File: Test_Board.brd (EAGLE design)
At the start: 63.5 x 57.1 mm, 33 parts, among them U1 Value, U2 Value

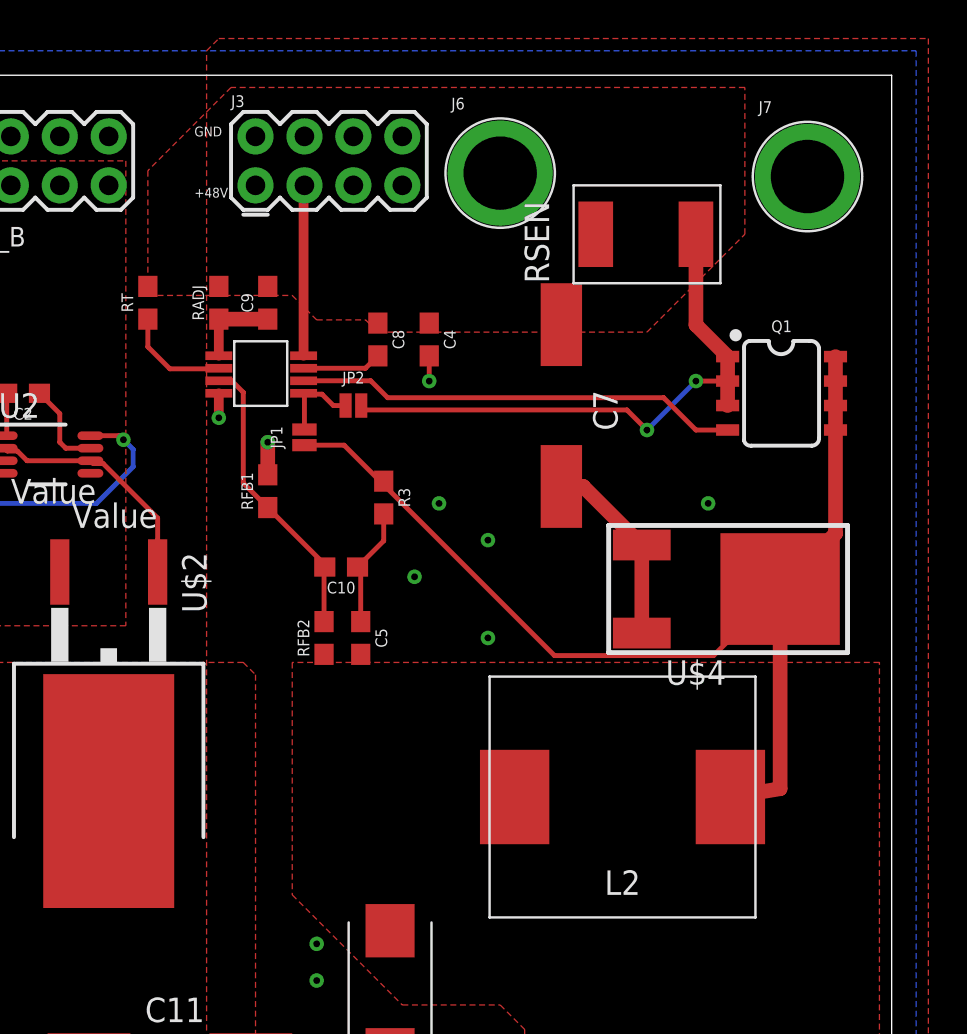
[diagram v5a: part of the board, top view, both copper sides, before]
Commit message: adjusted buck controller
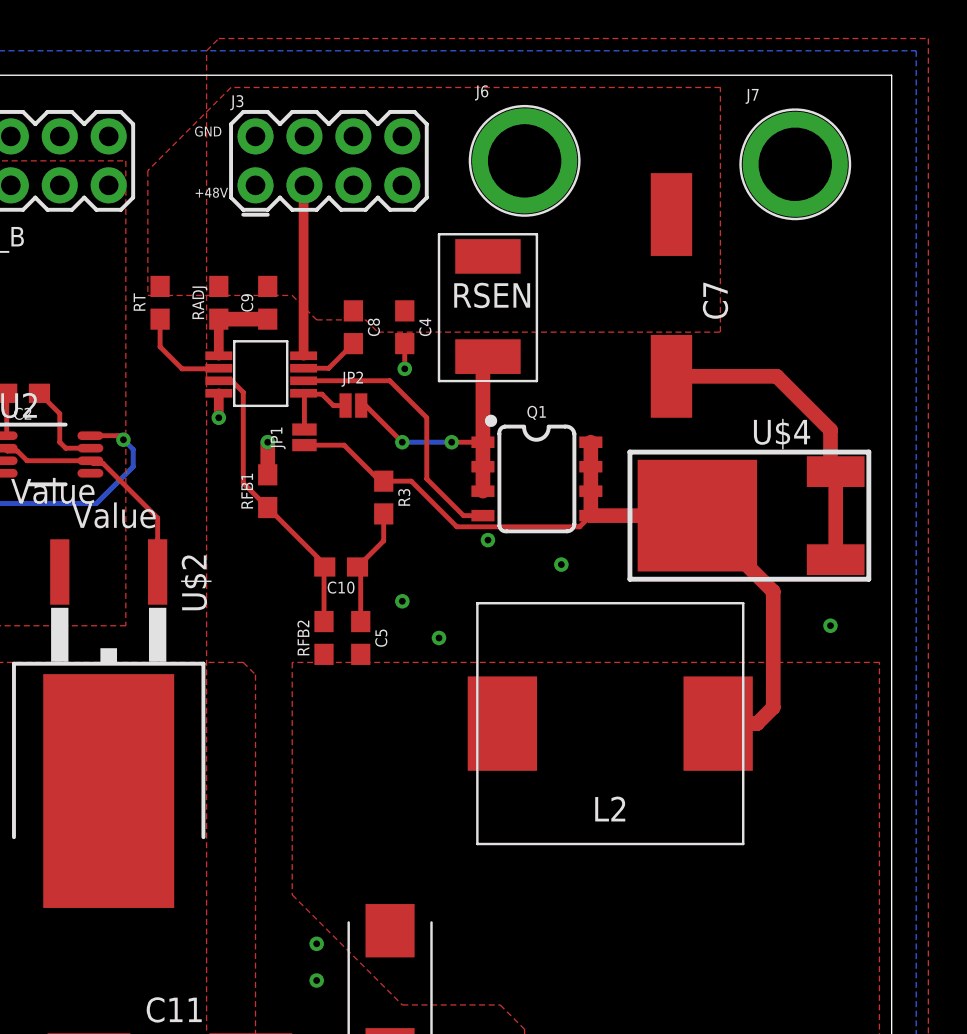
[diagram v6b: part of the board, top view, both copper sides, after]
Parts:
- moved Q1 13.5 mm to (32.4, 36.2)
- moved RSEN 12.5 mm to (29.8, 42.5), turned to 0 degrees
- moved C7 8.08 mm to (39.4, 45.7)
- moved U$4 4.26 mm to (43.8, 34.3), turned to 0 degrees
- moved L2 3.86 mm to (36.2, 23.5)
- moved C4 1.42 mm to (25.5, 44.1)
- moved C8 1.42 mm to (22.9, 44.1)
- moved J6 1.42 mm to (31.8, 52.7)
- moved J7 0.90 mm to (45.8, 52.5)
- moved RT 0.63 mm to (12.8, 45.3)
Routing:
- net N$11: track 57.1 -> 41.0 mm
- net N$14: track 30.2 -> 14.2 mm
- net GATE: track 23.1 -> 14.1 mm
- net GND: track 14.3 -> 20.5 mm
- net VCC: track 4.12 -> 3.11 mm
- net RT: track 5.60 -> 4.97 mm
